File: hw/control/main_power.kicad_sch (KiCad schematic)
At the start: 15 parts, among them U201 LM2596T-ADJ

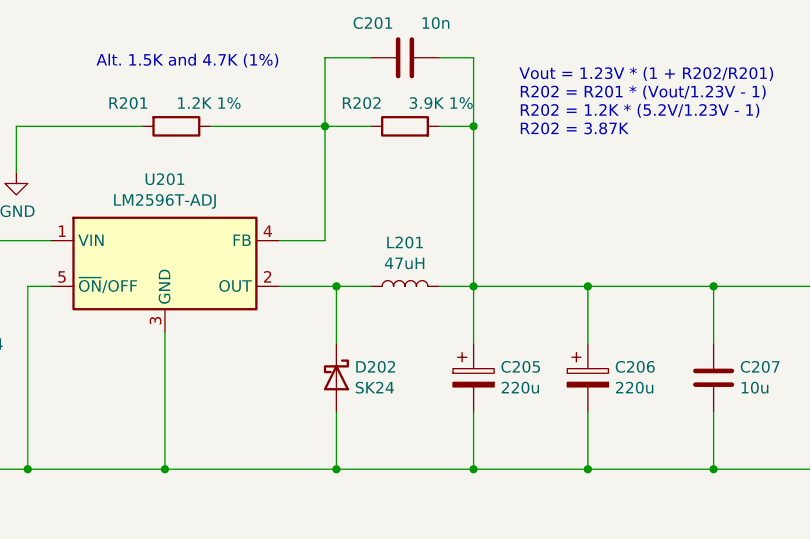
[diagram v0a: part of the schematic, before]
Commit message: [hw] Update to KiCAD 7
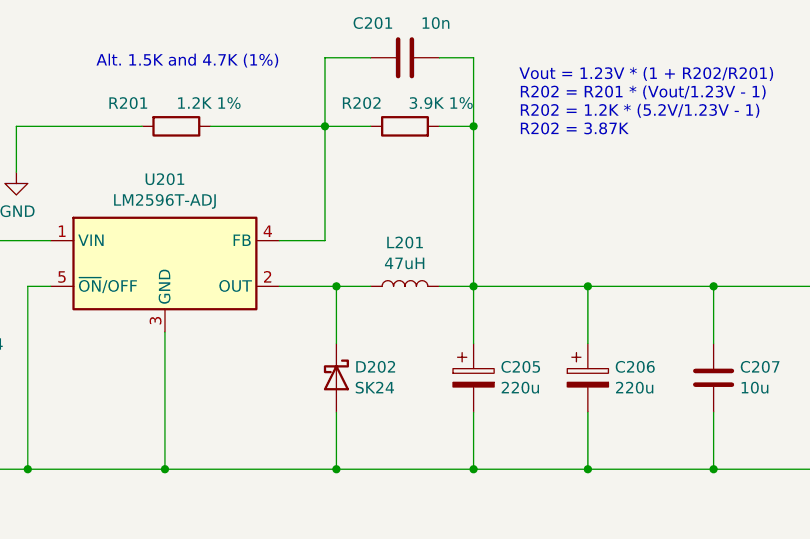
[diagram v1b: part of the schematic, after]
